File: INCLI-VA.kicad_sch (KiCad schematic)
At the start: 4 parts

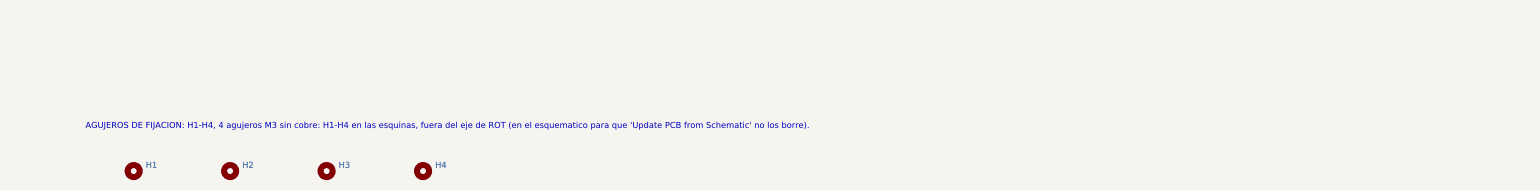
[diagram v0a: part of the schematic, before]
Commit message: [Claude Code] PCB: H1-H5 M3 metalizados sin red, apoyo B, barrera CAN, pinout y nombre en serigrafia
- H1-H4 a MountingHole_3.2mm_M3_Pad y H5 nuevo en (56.0, 38.5); simbolo sin pin,
  anillo flotante. Reglas H_anillo_cobre (0.5 mm) y H_zona_arandela (4 mm del centro).
- Rule area APOYO_CAJA_B (8 mm en B.Cu, 63.5/49.0): sin pistas/vias/pads, relleno permitido.
- Serigrafia 0.8/0.15: linea de barrera CAN y "CAN AISLADO" en ambas caras, pinout J1/J2,
  nombre/Rev/fecha abajo, rotulos de zona. Incluye el borrado de CAN_H/CAN_L del usuario.
- DRC 0 errores, paridad 0; ERC 0 errores; sch_visual_qa raiz PASS. Sin ruteo.

Co-Authored-By: Claude Opus 5.5 <noreply@anthropic.com>
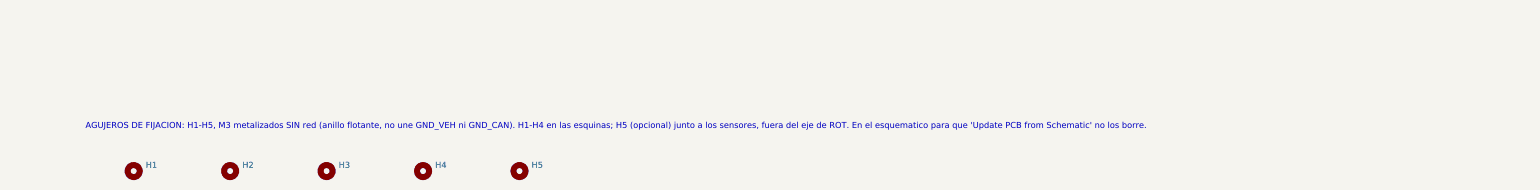
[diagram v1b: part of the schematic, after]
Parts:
- added H5: MountingHole_M3, MountingHole:MountingHole_3.2mm_M3_Pad, symbol Mechanical:MountingHole
- H1, H2, H3, H4: footprint MountingHole:MountingHole_3.2mm_M3 -> MountingHole:MountingHole_3.2mm_M3_Pad; MPN N/A (agujero NPTH) -> N/A (agujero PTH sin red); Notes Agujero de fijacion M3 (3.2 mm), SIN cobre (NPTH): separado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 -> Agujero de fijacion M3 (3.2 mm) metalizado, anillo de 6.4 m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
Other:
- note added: "AGUJEROS DE FIJACION: H1-H5, M3 metalizados SIN red (anillo flotante, no une GND_VEH ni GND_CAN). H1-H4 en las esquinas; H5 (opcional) junto a los sensores, fuera del eje de ROT. En el esquematico para que 'Update PCB from Schematic' no los borre."
- note removed: "AGUJEROS DE FIJACION: H1-H4, 4 agujeros M3 sin cobre: H1-H4 en las esquinas, fuera del eje de ROT (en el esquematico para que 'Update PCB from Schematic' no los borre)."
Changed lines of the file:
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@@
 		(comment 2 "Inclinómetro de chasis CAN/BLE — INCLI-VA")
 	)
-	(text "AGUJEROS DE FIJACION: H1-H4, 4 agujeros M3 sin cobre: H1-H4 en las esquinas, fuera del eje de ROT (en el esquematico para que 'Update PCB from Schematic' no los borre)."
+	(text "AGUJEROS DE FIJACION: H1-H5, M3 metalizados SIN red (anillo flotante, no une GND_VEH ni GND_CAN). H1-H4 en las esquinas; H5 (opcional) junto a los sensores, fuera del eje de ROT. En el esquematico para que 'Update PCB from Schematic' no los borre."
 		(exclude_from_sim no)
 		(at 50.8 246.38 0)
@@
 			)
 		)
-		(property "Footprint" "MountingHole:MountingHole_3.2mm_M3"
+		(property "Footprint" "MountingHole:MountingHole_3.2mm_M3_Pad"
 			(at 101.6 256.54 0)
 			(hide yes)
@@
 			)
 		)
-		(property "MPN" "N/A (agujero NPTH)"
+		(property "MPN" "N/A (agujero PTH sin red)"
 			(at 101.6 256.54 0)
 			(hide yes)
@@
 			)
 		)
-		(property "Notes" "Agujero de fijacion M3 (3.2 mm), SIN cobre (NPTH): separador plastico, no puentea dominios. Courtyard de 6.9 mm para arandela/cabeza. Posicion: la define el layout (ver docs/LAYOUT_NOTES.md)."
+		(property "Notes" "Agujero de fijacion M3 (3.2 mm) metalizado, anillo de 6.4 mm en ambas caras (huella oficial MountingHole_3.2mm_M3_Pad). SIN red: el simbolo no tiene pin, el anillo queda flotante y no une GND_VEH ni GND_CAN. Regla DRC: cobre a >= 0.5 mm del anillo y sin pistas ni vias a menos de 4 mm del centro (arandela). Posicion: ver docs/LAYOUT_NOTES.md."
 			(at 101.6 256.54 0)
 			(hide yes)
@@
 			)
 		)
-		(property "Footprint" "MountingHole:MountingHole_3.2mm_M3"
+		(property "Footprint" "MountingHole:MountingHole_3.2mm_M3_Pad"
 			(at 121.92 256.54 0)
 			(hide yes)
@@
 			)
 		)
-		(property "MPN" "N/A (agujero NPTH)"
+		(property "MPN" "N/A (agujero PTH sin red)"
 			(at 121.92 256.54 0)
 			(hide yes)
@@
 			)
 		)
-		(property "Notes" "Agujero de fijacion M3 (3.2 mm), SIN cobre (NPTH): separador plastico, no puentea dominios. Courtyard de 6.9 mm para arandela/cabeza. Posicion: la define el layout (ver docs/LAYOUT_NOTES.md)."
+		(property "Notes" "Agujero de fijacion M3 (3.2 mm) metalizado, anillo de 6.4 mm en ambas caras (huella oficial MountingHole_3.2mm_M3_Pad). SIN red: el simbolo no tiene pin, el anillo queda flotante y no une GND_VEH ni GND_CAN. Regla DRC: cobre a >= 0.5 mm del anillo y sin pistas ni vias a menos de 4 mm del centro (arandela). Posicion: ver docs/LAYOUT_NOTES.md."
 			(at 121.92 256.54 0)
 			(hide yes)
@@
 			)
 		)
-		(property "Footprint" "MountingHole:MountingHole_3.2mm_M3"
+		(property "Footprint" "MountingHole:MountingHole_3.2mm_M3_Pad"
 			(at 81.28 256.54 0)
 			(hide yes)
@@
 			)
 		)
-		(property "MPN" "N/A (agujero NPTH)"
+		(property "MPN" "N/A (agujero PTH sin red)"
 			(at 81.28 256.54 0)
 			(hide yes)
@@
 			)
 		)
-		(property "Notes" "Agujero de fijacion M3 (3.2 mm), SIN cobre (NPTH): separador plastico, no puentea dominios. Courtyard de 6.9 mm para arandela/cabeza. Posicion: la define el layout (ver docs/LAYOUT_NOTES.md)."
+		(property "Notes" "Agujero de fijacion M3 (3.2 mm) metalizado, anillo de 6.4 mm en ambas caras (huella oficial MountingHole_3.2mm_M3_Pad). SIN red: el simbolo no tiene pin, el anillo queda flotante y no une GND_VEH ni GND_CAN. Regla DRC: cobre a >= 0.5 mm del anillo y sin pistas ni vias a menos de 4 mm del centro (arandela). Posicion: ver docs/LAYOUT_NOTES.md."
 			(at 81.28 256.54 0)
 			(hide yes)
@@
 			)
 		)
-		(property "Footprint" "MountingHole:MountingHole_3.2mm_M3"
+		(property "Footprint" "MountingHole:MountingHole_3.2mm_M3_Pad"
 			(at 60.96 256.54 0)
 			(hide yes)
@@
 			)
 		)
-		(property "MPN" "N/A (agujero NPTH)"
+		(property "MPN" "N/A (agujero PTH sin red)"
 			(at 60.96 256.54 0)
 			(hide yes)
@@
 			)
 		)
-		(property "Notes" "Agujero de fijacion M3 (3.2 mm), SIN cobre (NPTH): separador plastico, no puentea dominios. Courtyard de 6.9 mm para arandela/cabeza. Posicion: la define el layout (ver docs/LAYOUT_NOTES.md)."
+		(property "Notes" "Agujero de fijacion M3 (3.2 mm) metalizado, anillo de 6.4 mm en ambas caras (huella oficial MountingHole_3.2mm_M3_Pad). SIN red: el simbolo no tiene pin, el anillo queda flotante y no une GND_VEH ni GND_CAN. Regla DRC: cobre a >= 0.5 mm del anillo y sin pistas ni vias a menos de 4 mm del centro (arandela). Posicion: ver docs/LAYOUT_NOTES.md."
 			(at 60.96 256.54 0)
 			(hide yes)
@@
 					(unit 1)
 				)
+			)
+		)
+	)
+	(symbol
+		(lib_id "Mechanical:MountingHole")
+		(at 142.24 256.54 0)
+		(unit 1)
+		(body_style 1)
+		(exclude_from_sim no)
+		(in_bom no)
+		(on_board yes)
+		(in_pos_files yes)
+		(dnp no)
+		(property "Reference" "H5"
+			(at 144.78 255.27 0)
+			(show_name no)
+			(do_not_autoplace no)
+			(effects
+				(font
+					(size 1.27 1.27)
+				)
+				(justify left)
+			)
+		)
+		(property "Value" "MountingHole_M3"
+			(at 144.78 257.81 0)
+			(hide yes)
+			(show_name no)
+			(do_not_autoplace no)
+			(effects
+				(font
+					(size 1.27 1.27)
+				)
+				(justify left)
+			)
+		)
+		(property "Footprint" "MountingHole:MountingHole_3.2mm_M3_Pad"
+			(at 142.24 256.54 0)
+			(hide yes)
+			(show_name no)
+			(do_not_autoplace no)
+			(effects
+				(font
+					(size 1.27 1.27)
+				)
+			)
+		)
+		(property "Datasheet" "https://www.kicad.org/libraries/"
+			(at 142.24 256.54 0)
+			(hide yes)
+			(show_name no)
+			(do_not_autoplace no)
+			(effects
+				(font
+					(size 1.27 1.27)
+				)
+			)
+		)
+		(property "Description" ""
+			(at 142.24 256.54 0)
+			(hide yes)
+			(show_name no)
+			(do_not_autoplace no)
+			(effects
+				(font
+					(size 1.27 1.27)
+				)
+			)
+		)
+		(property "MPN" "N/A (agujero PTH sin red)"
+			(at 142.24 256.54 0)
+			(hide yes)
+			(show_name no)
+			(do_not_autoplace no)
+			(effects
+				(font
+					(size 1.27 1.27)
+				)
+			)
+		)
+		(property "Manufacturer" "N/A"
+			(at 142.24 256.54 0)
+			(hide yes)
+			(show_name no)
+			(do_not_autoplace no)
+			(effects
+				(font
+					(size 1.27 1.27)
+				)
+			)
+		)
+		(property "DNP" ""
+			(at 142.24 256.54 0)
+			(hide yes)
+			(show_name no)
+			(do_not_autoplace no)
+			(effects
+				(font
+					(size 1.27 1.27)
+				)
+			)
+		)
+		(property "Notes" "Agujero de fijacion M3 (3.2 mm) metalizado, anillo de 6.4 mm en ambas caras (huella oficial MountingHole_3.2mm_M3_Pad). SIN red: el simbolo no tiene pin, el anillo queda flotante y no une GND_VEH ni GND_CAN. Regla DRC: cobre a >= 0.5 mm del anillo y sin pistas ni vias a menos de 4 mm del centro (arandela). Posicion: ver docs/LAYOUT_NOTES.md."
+			(at 142.24 256.54 0)
+			(hide yes)
+			(show_name no)
+			(do_not_autoplace no)
+			(effects
+				(font
+					(size 1.27 1.27)
+				)
+			)
+		)
+		(instances
+			(project "INCLI-VA"
+				(path "/7fd92c2b-4254-4d73-93ba-bfde861bede3"
+					(reference "H5")
+					(unit 1)
+				)

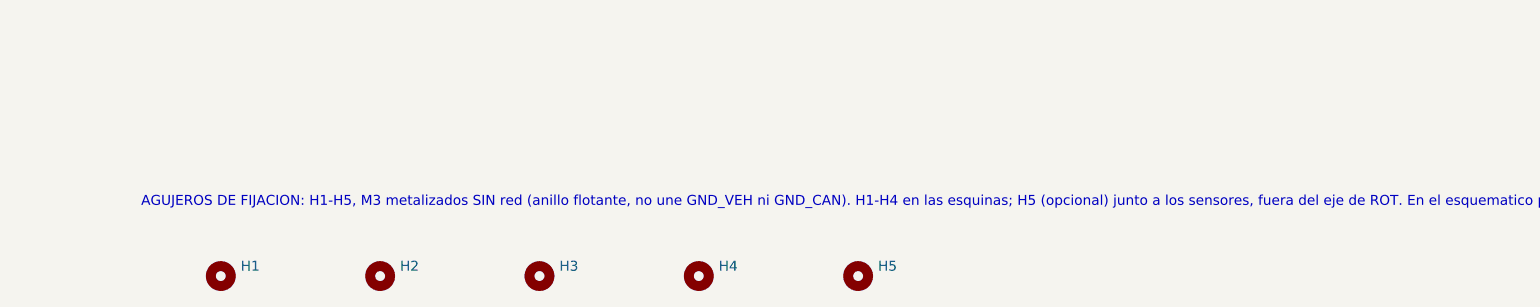
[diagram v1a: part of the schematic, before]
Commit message: [Claude Code] PCB: fiduciales FID1–FID3, relleno/teardrops, máscara roja, fab regenerado (pcb-v1-rc3)
- FID1–FID3 (Fiducial_1mm_Mask2mm, F.Cu, sin red, fuera de BOM/CPL) en
  esquema raíz y PCB; etapa6_fiduciales.py.
- Relleno de zonas: vuelven los 5 teardrops perdidos en «update serigrafia»;
  DRC 0 errores / 3 avisos aceptados, paridad 0, ERC 0 / 5 avisos.
- Máscara roja: puentes ≥ 0.15 mm (U502) contra 0.10 mm de JLC (1 oz).
- fab/proto regenerado. LCSC: sustitutos C303 y C601/C607 (VERIFY).
- Logos en B.Silkscreen pendientes para rc4 (faltan los archivos).

Co-Authored-By: Claude Opus 5.5 <noreply@anthropic.com>
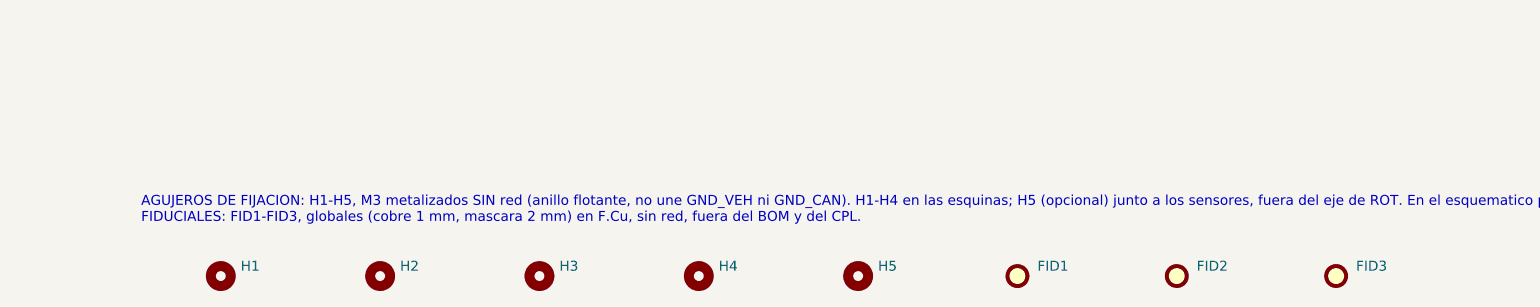
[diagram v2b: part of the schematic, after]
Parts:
- added FID1, FID2, FID3: Fiducial, Fiducial:Fiducial_1mm_Mask2mm, symbol Mechanical:Fiducial
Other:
- note added: "AGUJEROS DE FIJACION: H1-H5, M3 metalizados SIN red (anillo flotante, no une GND_VEH ni GND_CAN). H1-H4 en las esquinas; H5 (opcional) junto a los sensores, fuera del eje de ROT. En el esquematico para que 'Update PCB from Schematic' no los borre. FIDUCIALES: FID1-FID3, globales (cobre 1 mm, mascara 2 mm) en F.Cu, sin red, fuera del BOM y del CPL."
- note removed: "AGUJEROS DE FIJACION: H1-H5, M3 metalizados SIN red (anillo flotante, no une GND_VEH ni GND_CAN). H1-H4 en las esquinas; H5 (opcional) junto a los sensores, fuera del eje de ROT. En el esquematico para que 'Update PCB from Schematic' no los borre."
